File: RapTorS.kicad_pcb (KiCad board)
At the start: 2 copper layers, 22 parts, among them J1 Molex 48037-2200, J2 TestPoint, J3 TestPoint, J4 TestPoint, J5 TestPoint, J6 TestPoint, U1 PIC16LF1454-I_ML, U2 TLV71333PDBV, U3 E07-M1101S

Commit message: first placement
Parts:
- moved J1 78.2 mm to (2.75, 9.50), turned to 270 degrees
- moved U3 41.2 mm to (24.8, 2.79)
- moved ANT1 24.3 mm to (62.3, 25.6)
- moved J3 21.4 mm to (62.2, 33.0)
- moved U1 21.3 mm to (52.0, 35.7)
- moved J6 20.1 mm to (70.1, 26.7)
- moved J4 15.5 mm to (70.1, 32.7)
- moved R2 14.4 mm to (63.0, 38.1)
- moved C2 14.0 mm to (44.1, 56.3)
- moved R1 13.9 mm to (57.6, 44.2)
- moved J5 13.6 mm to (78.4, 32.6)
- moved D2 11.6 mm to (51.6, 44.5)
- moved C5 11.1 mm to (50.7, 56.2)
- moved R3 10.3 mm to (63.5, 44.0)
- moved C3 8.75 mm to (44.4, 48.5)
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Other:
- board outline added: 45 x 19 mm
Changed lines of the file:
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@@
   (general
     (thickness 1.6)
-    (drawings 0)
+    (drawings 4)
     (tracks 0)
     (zones 0)
@@
     (pad_to_mask_clearance 0.2)
     (aux_axis_origin 0 0)
-    (visible_elements FFFFFF7F)
+    (visible_elements FEFFF77F)
     (pcbplotparams
       (layerselection 0x010fc_ffffffff)
@@
   )
   (module Capacitors_SMD:CP_Elec_4x4.5 (layer F.Cu)
-    (at 52.727201 51.228801)
+    (at 44.3992 48.5394)
     (descr "SMT capacitor, aluminium electrolytic, 4x4.5")
     (attr smd)
@@
   )
   (module Capacitors_SMD:C_0805 (layer F.Cu)
-    (at 57.877201 51.463801)
+    (at 56.7182 55.9562)
     (descr "Capacitor SMD 0805, reflow soldering, AVX (see smccp.pdf)")
     (tags "capacitor 0805")
@@
   )
   (module Capacitors_SMD:C_0805 (layer F.Cu)
-    (at 61.427201 53.283801)
+    (at 50.6984 56.1848)
     (descr "Capacitor SMD 0805, reflow soldering, AVX (see smccp.pdf)")
     (tags "capacitor 0805")
@@
   )
   (module Capacitors_SMD:C_0805 (layer F.Cu)
-    (at 61.427201 51.463801)
+    (at 57.6072 49.7332)
     (descr "Capacitor SMD 0805, reflow soldering, AVX (see smccp.pdf)")
     (tags "capacitor 0805")
@@
   )
   (module Capacitors_SMD:C_0805 (layer F.Cu)
-    (at 57.877201 53.363801)
+    (at 44.1452 56.2864)
     (descr "Capacitor SMD 0805, reflow soldering, AVX (see smccp.pdf)")
     (tags "capacitor 0805")
@@
   )
   (module Capacitors_SMD:C_0805 (layer F.Cu)
-    (at 69.627201 49.713801)
+    (at 63.5508 49.9872)
     (descr "Capacitor SMD 0805, reflow soldering, AVX (see smccp.pdf)")
     (tags "capacitor 0805")
@@
   )
   (module Connectors:Pin_d1.0mm_L10.0mm (layer F.Cu)
-    (at 78.797201 43.418801)
+    (at 62.2554 25.6286)
     (descr "solder Pin_ diameter 1.0mm, hole diameter 1.0mm (press fit), length 10.0mm")
     (tags "solder Pin_ press fit")
@@
   )
   (module Connectors_TestPoints:Test_Point_Pad_1.5x1.5mm (layer F.Cu)
-    (at 75.827201 49.648801)
+    (at 69.6722 43.7896)
     (descr "SMD rectangular pad as test Point, square 1.5mm side length")
     (tags "test point SMD pad rectangle square")
@@
   )
   (module Connectors_TestPoints:Test_Point_Pad_d1.5mm (layer F.Cu)
-    (at 81.597201 43.168801)
+    (at 70.0532 26.7462)
     (descr "SMD pad as test Point, diameter 1.5mm")
     (tags "test point SMD pad")
@@
   )
   (module Connectors_TestPoints:Test_Point_Pad_d1.5mm (layer F.Cu)
-    (at 78.447201 46.218801)
+    (at 78.4098 32.5882)
     (descr "SMD pad as test Point, diameter 1.5mm")
     (tags "test point SMD pad")
@@
   )
   (module Connectors_TestPoints:Test_Point_Pad_d1.5mm (layer F.Cu)
-    (at 75.827201 47.098801)
+    (at 70.0532 32.7152)
     (descr "SMD pad as test Point, diameter 1.5mm")
     (tags "test point SMD pad")
@@
   )
   (module Connectors_TestPoints:Test_Point_Pad_d1.5mm (layer F.Cu)
-    (at 72.277201 51.898801)
+    (at 62.2046 32.9692)
     (descr "SMD pad as test Point, diameter 1.5mm")
     (tags "test point SMD pad")
@@
   )
   (module E07-M1101S:E07-M1101S (layer F.Cu)
-    (at 49.6022 35.7338)
+    (at 24.8412 2.794)
     (fp_text reference U3 (at 11.811 4.445) (layer F.SilkS)
       (effects (font (size 1 1) (thickness 0.15)))
@@
   )
   (module Housings_DFN_QFN:QFN-16-1EP_4x4mm_Pitch0.65mm (layer F.Cu)
-    (at 71.347201 44.568801)
+    (at 51.9938 35.7124)
     (descr "16-Lead Plastic Quad Flat, No Lead Package (ML) - 4x4x0.9 mm Body [QFN]; (see Microchip Packaging Specification 00000049BS.pdf)")
     (tags "QFN 0.65")
@@
   )
   (module Inductors_SMD:L_0805 (layer F.Cu)
-    (at 75.647201 42.918801)
+    (at 69.1744 38.2016)
     (descr "Resistor SMD 0805, reflow soldering, Vishay (see dcrcw.pdf)")
     (tags "resistor 0805")
@@
   )
   (module LEDs:LED_0805 (layer F.Cu)
-    (at 62.027201 49.678801)
+    (at 51.605 44.5262)
     (descr "LED 0805 smd package")
     (tags "LED led 0805 SMD smd SMT smt smdled SMDLED smtled SMTLED")
@@
   )
   (module LEDs:LED_0805 (layer F.Cu)
-    (at 58.077201 49.678801)
+    (at 51.0794 50.038)
     (descr "LED 0805 smd package")
     (tags "LED led 0805 SMD smd SMT smt smdled SMDLED smtled SMTLED")
@@
   )
   (module PX_Molex:MOLEX_USB_48037-2200 (layer F.Cu)
-    (at 75.1722 39.0838)
-    (attr smd)
-    (fp_text reference J1 (at 10.668 -7.62) (layer F.SilkS)
-      (effects (font (size 1 1) (thickness 0.15)))
-    )
-    (fp_text value "Molex 48037-2200" (at 3.556 -5.588) (layer F.Fab)
+    (at 2.75 9.5 270)
+    (attr smd)
+    (fp_text reference J1 (at 10.668 -7.62 270) (layer F.SilkS)
+      (effects (font (size 1 1) (thickness 0.15)))
+    )
+    (fp_text value "Molex 48037-2200" (at 3.556 -5.588 270) (layer F.Fab)
       (effects (font (size 1 1) (thickness 0.15)))
     )
     (fp_line (start -6 2.75) (end 6 2.75) (layer F.Fab) (width 0.12))
-    (pad 2 smd rect (at 1 -2.6) (size 1.2 2) (layers F.Cu F.Paste F.Mask)
+    (pad 2 smd rect (at 1 -2.6 270) (size 1.2 2) (layers F.Cu F.Paste F.Mask)
       (net 10 D-))
-    (pad 1 smd rect (at 3.5 -2.6) (size 1.2 2) (layers F.Cu F.Paste F.Mask)
+    (pad 1 smd rect (at 3.5 -2.6 270) (size 1.2 2) (layers F.Cu F.Paste F.Mask)
       (net 11 "Net-(C1-Pad1)"))
-    (pad 3 smd rect (at -1 -2.6) (size 1.2 2) (layers F.Cu F.Paste F.Mask)
+    (pad 3 smd rect (at -1 -2.6 270) (size 1.2 2) (layers F.Cu F.Paste F.Mask)
       (net 12 D+))
-    (pad 4 smd rect (at -3.5 -2.6) (size 1.2 2) (layers F.Cu F.Paste F.Mask)
-      (net 4 GND))
-    (pad "" np_thru_hole circle (at 2.25 0) (size 1.1 1.1) (drill 1.1) (layers *.Cu *.Mask))
-    (pad "" np_thru_hole circle (at -2.25 0) (size 1.1 1.1) (drill 1.1) (layers *.Cu *.Mask))
-    (pad 5 thru_hole roundrect (at -5.85 0) (size 1.3 3.2) (drill oval 0.7 2.5) (layers *.Cu *.Mask) (roundrect_rratio 0.5)
+    (pad 4 smd rect (at -3.5 -2.6 270) (size 1.2 2) (layers F.Cu F.Paste F.Mask)
+      (net 4 GND))
+    (pad "" np_thru_hole circle (at 2.25 0 270) (size 1.1 1.1) (drill 1.1) (layers *.Cu *.Mask))
+    (pad "" np_thru_hole circle (at -2.25 0 270) (size 1.1 1.1) (drill 1.1) (layers *.Cu *.Mask))
+    (pad 5 thru_hole roundrect (at -5.85 0 270) (size 1.3 3.2) (drill oval 0.7 2.5) (layers *.Cu *.Mask) (roundrect_rratio 0.5)
       (net 5 "Net-(J1-Pad5)"))
-    (pad 5 thru_hole roundrect (at 5.85 0) (size 1.3 3.2) (drill oval 0.7 2.5) (layers *.Cu *.Mask) (roundrect_rratio 0.5)
+    (pad 5 thru_hole roundrect (at 5.85 0 270) (size 1.3 3.2) (drill oval 0.7 2.5) (layers *.Cu *.Mask) (roundrect_rratio 0.5)
       (net 5 "Net-(J1-Pad5)"))
     (model "${KIPRJMOD}/3d_models/Molex 480372-200.step"
@@
   )
   (module Resistors_SMD:R_0805 (layer F.Cu)
-    (at 72.977201 48.183801)
+    (at 63.5356 44.0436)
     (descr "Resistor SMD 0805, reflow soldering, Vishay (see dcrcw.pdf)")
     (tags "resistor 0805")
@@
   )
   (module Resistors_SMD:R_0805 (layer F.Cu)
-    (at 75.597201 44.883801)
+    (at 62.9514 38.0746)
     (descr "Resistor SMD 0805, reflow soldering, Vishay (see dcrcw.pdf)")
     (tags "resistor 0805")
@@
   )
   (module Resistors_SMD:R_0805 (layer F.Cu)
-    (at 69.427201 51.563801)
+    (at 57.6072 44.2468)
     (descr "Resistor SMD 0805, reflow soldering, Vishay (see dcrcw.pdf)")
     (tags "resistor 0805")
@@
   )
   (module TO_SOT_Packages_SMD:SOT-23-5 (layer F.Cu)
-    (at 65.927201 50.628801)
+    (at 64.008 57.2262)
     (descr "5-pin SOT23 package")
     (tags SOT-23-5)
@@
     )
   )
+  (gr_line (start 0 0) (end 0 19) (layer Edge.Cuts) (width 0.12))
+  (gr_line (start 45 19) (end 0 19) (layer Edge.Cuts) (width 0.12))
+  (gr_line (start 45 0) (end 45 19) (layer Edge.Cuts) (width 0.12))
+  (gr_line (start 0 0) (end 45 0) (layer Edge.Cuts) (width 0.12))
 )

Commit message: placement second step
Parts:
- removed C5: 100nF, Capacitors_SMD:C_0805
- J2: footprint Connectors_TestPoints:Test_Point_Pad_1.5x1.5mm -> Connectors_TestPoints:Test_Point_Pad_d1.5mm
- moved J1 166.0 mm to (141.5, 100.7)
- moved U3 163.5 mm to (162.0, 91.8)
- moved ANT1 142.6 mm to (179.7, 106.6)
- moved D1 141.7 mm to (182.5, 103.1), turned to 270 degrees
- moved D2 141.6 mm to (182.5, 98.5), turned to 90 degrees
- moved R2 138.0 mm to (182.5, 107.1), turned to 90 degrees
- moved R3 129.3 mm to (182.5, 94.6), turned to 270 degrees
- moved C3 124.0 mm to (154.3, 106.1), turned to 270 degrees
- moved C6 122.8 mm to (168.1, 107.5), turned to 270 degrees
- moved U1 118.8 mm to (152.7, 98.8), turned to 180 degrees
- moved C2 117.7 mm to (150.3, 107.2), turned to 270 degrees
- moved U2 112.9 mm to (165.0, 107.6)
- moved C4 112.1 mm to (157.4, 100.8)
- moved J6 111.5 mm to (159.7, 93.1)
- moved R1 105.9 mm to (141.5, 108.8)
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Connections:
- U2 pad 4: Net-(U2-Pad4) -> (no net)
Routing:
- net D-: track 0.00 -> 22.0 mm
- net D+: track 0.00 -> 20.8 mm
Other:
- net class Default: clearance 0.2 -> 0.16
- rule trace_clearance: 0.2 -> 0.16
- rule trace_min: 0.2 -> 0.16

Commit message: routing OK
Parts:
- J2, J3, J4, J5, J6: moved to B.Cu
- moved C4 10.7 mm to (146.7, 101.1), turned to 270 degrees
- moved C1 3.88 mm to (148.0, 105.7)
- moved L1 3.88 mm to (151.0, 104.9)
- moved C2 3.88 mm to (153.9, 105.8)
- moved C3 3.77 mm to (158.0, 105.8)
- moved R1 3.59 mm to (144.9, 107.5), turned to 270 degrees
- moved J2 2.62 mm to (148.0, 92.5)
- moved U1 2.08 mm to (150.6, 98.8), turned to 90 degrees
- moved J6 1.64 mm to (158.2, 92.5)
- moved J3 1.53 mm to (150.5, 92.5)
- moved U2 1.12 mm to (163.9, 107.4)
- moved J4 0.84 mm to (153.1, 92.5)
- moved J5 0.56 mm to (155.6, 92.5)
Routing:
- net +3V3: track 0.00 -> 55.3 mm, vias 0 -> 3
- net LED: track 0.00 -> 38.4 mm, vias 0 -> 2
- net LED_DEBUG: track 0.00 -> 37.9 mm, vias 0 -> 2
- net CSN: track 0.00 -> 20.8 mm, vias 0 -> 2
- net ISPCLK: track 0.00 -> 19.2 mm, vias 0 -> 2
- net Net-(J1-Pad5): track 0.00 -> 19.0 mm
- net ~MCLR: track 0.00 -> 16.7 mm, vias 0 -> 1
- net ISPDAT: track 0.00 -> 16.5 mm, vias 0 -> 1
- net +5V: track 0.00 -> 16.0 mm
- net GDO0: track 0.00 -> 14.7 mm, vias 0 -> 2
- net GDO2: track 0.00 -> 11.1 mm
- net MOSI: track 0.00 -> 10.6 mm
- net GND: track 0.00 -> 9.10 mm, vias 0 -> 37
- net Net-(C1-Pad1): track 0.00 -> 6.19 mm
- net Net-(ANT1-Pad1): track 0.00 -> 3.20 mm
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- added copper zone on B.Cu, net GND
- added copper zone on F.Cu, net GND

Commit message: add the logo
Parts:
- added G***: LOGO, Logo:Logo, B.Cu at (163.9, 99.5)

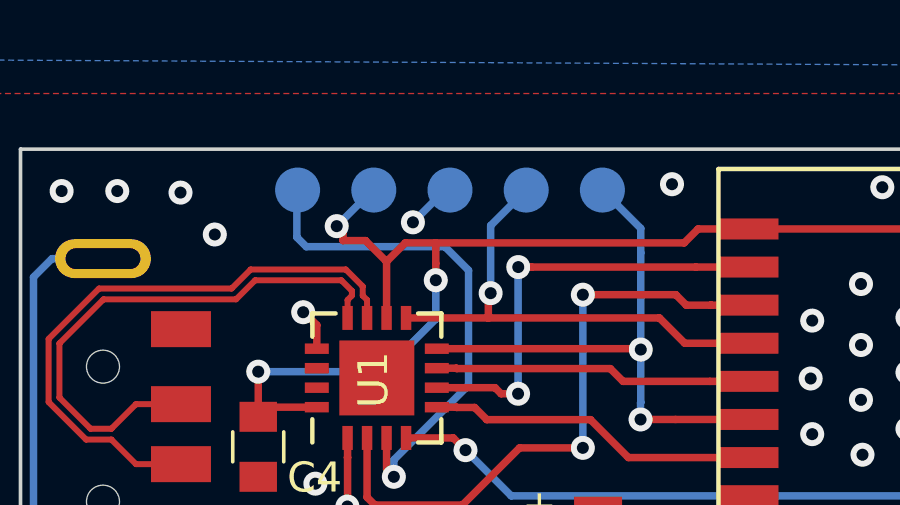
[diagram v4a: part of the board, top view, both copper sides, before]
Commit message: update logo size
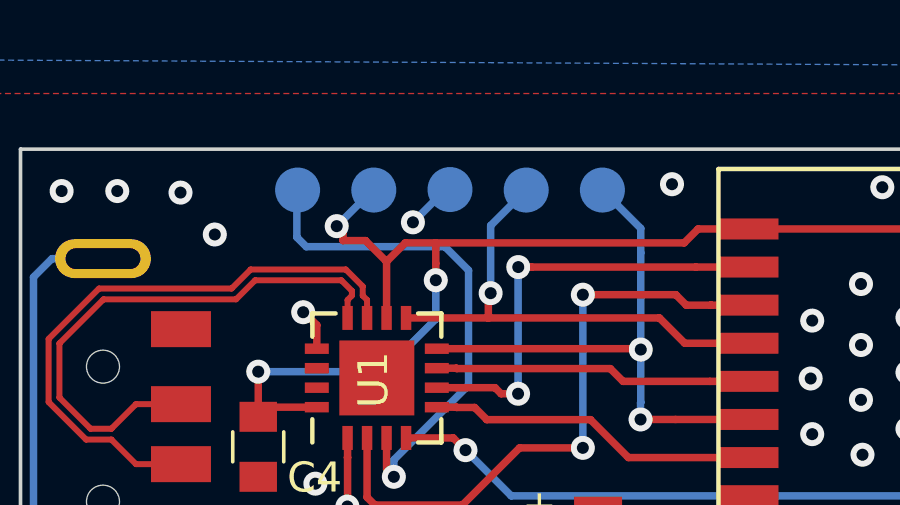
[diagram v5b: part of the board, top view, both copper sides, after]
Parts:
- moved G*** 1.44 mm to (163.0, 100.6)
